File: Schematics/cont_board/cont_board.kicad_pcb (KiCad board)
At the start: 2 copper layers, 238 x 67 mm, 45 parts, among them IC1 LM2931AZ-5.0_TO92, J1 Conn_01x04, J2 Conn_01x04, J3 Conn_01x04, J4 Conn_01x04, Q1 BD438, Q2 BD438, Q3 BD438, SW1 SW_SPDT, U1 LM317_TO-220, U2 MCP23017_SP, U3 ULN2803A, U4 MCP23017_SP, U5 ULN2803A

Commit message: Lamp Board Schematic started
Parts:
- moved H6 22.0 mm to (174.5, 83.5)
- moved H4 20.0 mm to (118.5, 103.5)
- moved U4 9.52 mm to (186.1, 66.0)
- moved JP4 5.85 mm to (188.0, 108.6)
- moved JP5 5.85 mm to (188.0, 111.8)
- moved JP6 5.85 mm to (188.0, 114.9)
- moved U5 4.44 mm to (200.7, 92.7)
- moved U3 4.44 mm to (200.7, 66.0)
- moved C6 0.63 mm to (124.5, 92.1)
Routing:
- net +5V: track 312.4 -> 333.8 mm, vias 3 -> 2
- net SCL: track 181.5 -> 194.8 mm, vias 3 -> 4
- net SDA: track 181.8 -> 194.4 mm, vias 1 -> 2
- net GND: track 26.5 -> 14.7 mm
- net LC6: track 58.6 -> 51.0 mm, vias 1 -> 0
- net LC9: track 41.1 -> 34.3 mm
- net CAM2_POS: track 94.7 -> 99.9 mm
- net LC2: track 14.1 -> 9.09 mm
- net LC3: track 14.1 -> 9.09 mm
- net LC1: track 14.1 -> 9.09 mm
- net LR1: track 22.6 -> 18.0 mm
- net /lamp_drive/c7: track 64.4 -> 60.0 mm
- net /lamp_drive/c5: track 64.8 -> 60.4 mm
- net /lamp_drive/r1: track 28.7 -> 24.3 mm
- net /lamp_drive/c6: track 64.4 -> 60.0 mm
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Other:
- board text added: "04/12/2023 - last rev. 07/12/2023"
- board text added: "CUED | LZB - Enigma Control Board v1.2"
- board text removed: "04/12/2023 - last rev. 06/12/2023"
- board text removed: "CUED | LZB - Enigma Control Board v1.1"

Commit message: Lamp Board Work and drl2dxf
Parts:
- moved H4 5.00 mm to (118.5, 108.5)
- moved H6 2.00 mm to (174.5, 85.5)
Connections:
- net Net-(IC1-VI) renamed /smth
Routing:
- net CAM2_POS: track 99.9 -> 94.2 mm
- net TEST_SW: track 136.4 -> 133.1 mm
- net +12V: track 47.4 -> 46.8 mm
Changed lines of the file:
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@@
   (net 105 "unconnected-(A1-PadVIN)")
   (net 106 "/lamp_drive/hp_r2")
-  (net 107 "Net-(IC1-VI)")
+  (net 107 "/smth")
   (net 108 "/s_a2")
   (net 109 "/s_a1")
@@
   )
   (footprint "MountingHole:MountingHole_3.2mm_M3_Pad_Via" (layer "F.Cu")
-    (at 118.5 103.5)
+    (at 118.5 108.5)
     (descr "Mounting Hole 3.2mm, M3")
     (tags "mounting hole 3.2mm m3")
@@
       (net 8 "+12V") (pintype "passive"))
     (pad "2" thru_hole oval (at 10.16 0 90) (size 1.6 1.6) (drill 0.8) (layers "*.Cu" "*.Mask")
-      (net 107 "Net-(IC1-VI)") (pintype "passive"))
+      (net 107 "/smth") (pintype "passive"))
     (model "${KICAD6_3DMODEL_DIR}/Resistor_THT.3dshapes/R_Axial_DIN0207_L6.3mm_D2.5mm_P10.16mm_Horizontal.wrl"
       (offset (xyz 0 0 0))
@@
       (stroke (width 0.1) (type solid)) (layer "F.Fab"))
     (pad "1" thru_hole circle (at 0 0 90) (size 1.6 1.6) (drill 0.8) (layers "*.Cu" "*.Mask")
-      (net 107 "Net-(IC1-VI)") (pintype "passive"))
+      (net 107 "/smth") (pintype "passive"))
     (pad "2" thru_hole circle (at 5 0 90) (size 1.6 1.6) (drill 0.8) (layers "*.Cu" "*.Mask")
       (net 1 "GND") (pintype "passive"))
@@
   )
   (footprint "MountingHole:MountingHole_3.2mm_M3_Pad_Via" (layer "F.Cu")
-    (at 174.5 83.5)
+    (at 174.5 85.5)
     (descr "Mounting Hole 3.2mm, M3")
     (tags "mounting hole 3.2mm m3")
@@
       (net 1 "GND") (pinfunction "GND") (pintype "power_in"))
     (pad "3" thru_hole oval (at 2.54 0 270) (size 1.05 1.5) (drill 0.75) (layers "*.Cu" "*.Mask")
-      (net 107 "Net-(IC1-VI)") (pinfunction "VI") (pintype "power_in"))
+      (net 107 "/smth") (pinfunction "VI") (pintype "power_in"))
     (model "${KICAD6_3DMODEL_DIR}/Package_TO_SOT_THT.3dshapes/TO-92_Inline.wrl"
       (offset (xyz 0 0 0))
@@
   (via (at 182.88 91.44) (size 1.2) (drill 0.6) (layers "F.Cu" "B.Cu") (free) (net 1))
   (via (at 231.14 80.09) (size 1.2) (drill 0.6) (layers "F.Cu" "B.Cu") (free) (net 1))
+  (segment (start 125.73 101.6) (end 125.73 102.87) (width 0.5) (layer "F.Cu") (net 2))
+  (segment (start 130.81 107.95) (end 132.08 107.95) (width 0.5) (layer "F.Cu") (net 2))
   (segment (start 132.08 107.95) (end 135.89 104.14) (width 0.5) (layer "F.Cu") (net 2))
-  (segment (start 125.73 107.315) (end 126.365 107.95) (width 0.5) (layer "F.Cu") (net 2))
-  (segment (start 126.365 107.95) (end 132.08 107.95) (width 0.5) (layer "F.Cu") (net 2))
   (segment (start 135.89 104.14) (end 135.89 92.075) (width 0.5) (layer "F.Cu") (net 2))
-  (segment (start 125.73 100.33) (end 125.73 107.315) (width 0.5) (layer "F.Cu") (net 2))
+  (segment (start 125.73 102.87) (end 130.81 107.95) (width 0.5) (layer "F.Cu") (net 2))
   (via (at 135.89 92.075) (size 0.8) (drill 0.4) (layers "F.Cu" "B.Cu") (net 2))
-  (via (at 125.73 100.33) (size 0.8) (drill 0.4) (layers "F.Cu" "B.Cu") (net 2))
-  (segment (start 86.36 106.68) (end 77.47 115.57) (width 0.5) (layer "B.Cu") (net 2))
-  (segment (start 91.44 104.14) (end 88.9 106.68) (width 0.5) (layer "B.Cu") (net 2))
+  (via (at 125.73 101.6) (size 0.8) (drill 0.4) (layers "F.Cu" "B.Cu") (net 2))
+  (segment (start 125.095 101.6) (end 118.11 94.615) (width 0.5) (layer "B.Cu") (net 2))
   (segment (start 138.43 89.535) (end 143.51 89.535) (width 0.5) (layer "B.Cu") (net 2))
-  (segment (start 50.8 115.57) (end 53.34 113.03) (width 0.5) (layer "B.Cu") (net 2))
   (segment (start 118.11 94.615) (end 97.79 94.615) (width 0.5) (layer "B.Cu") (net 2))
+  (segment (start 50.8 115.57) (end 53.34 113.03) (width 0.5) (layer "B.Cu") (net 2))
+  (segment (start 125.73 101.6) (end 125.095 101.6) (width 0.5) (layer "B.Cu") (net 2))
   (segment (start 77.47 115.57) (end 50.8 115.57) (width 0.5) (layer "B.Cu") (net 2))
   (segment (start 50.8 115.57) (end 47.27 119.1) (width 0.5) (layer "B.Cu") (net 2))
-  (segment (start 123.825 100.33) (end 118.11 94.615) (width 0.5) (layer "B.Cu") (net 2))
-  (segment (start 47.27 119.1) (end 47.27 119.38) (width 0.5) (layer "B.Cu") (net 2))
   (segment (start 97.79 94.615) (end 91.44 100.965) (width 0.5) (layer "B.Cu") (net 2))
+  (segment (start 47.27 119.1) (end 47.27 119.38) (width 0.5) (layer "B.Cu") (net 2))
   (segment (start 91.44 100.965) (end 91.44 104.14) (width 0.5) (layer "B.Cu") (net 2))
-  (segment (start 135.89 92.075) (end 138.43 89.535) (width 0.5) (layer "B.Cu") (net 2))
+  (segment (start 86.36 106.68) (end 77.47 115.57) (width 0.5) (layer "B.Cu") (net 2))
   (segment (start 88.9 106.68) (end 86.36 106.68) (width 0.5) (layer "B.Cu") (net 2))
-  (segment (start 125.73 100.33) (end 123.825 100.33) (width 0.5) (layer "B.Cu") (net 2))
+  (segment (start 91.44 104.14) (end 88.9 106.68) (width 0.5) (layer "B.Cu") (net 2))
+  (segment (start 135.89 92.075) (end 138.43 89.535) (width 0.5) (layer "B.Cu") (net 2))
   (segment (start 134.62 90.805) (end 135.89 89.535) (width 0.5) (layer "F.Cu") (net 3))
   (segment (start 131.38 105.98) (end 132.145 105.98) (width 0.5) (layer "F.Cu") (net 3))
@@
   (via (at 132.08 104.14) (size 0.8) (drill 0.4) (layers "F.Cu" "B.Cu") (net 4))
   (via (at 133.35 87.63) (size 0.8) (drill 0.4) (layers "F.Cu" "B.Cu") (net 4))
-  (segment (start 109.22 97.155) (end 112.395 100.33) (width 0.5) (layer "B.Cu") (net 4))
-  (segment (start 115.57 107.95) (end 128.27 107.95) (width 0.5) (layer "B.Cu") (net 4))
-  (segment (start 128.27 107.95) (end 132.08 104.14) (width 0.5) (layer "B.Cu") (net 4))
   (segment (start 95.885 103.505) (end 102.235 97.155) (width 0.5) (layer "B.Cu") (net 4))
+  (segment (start 102.235 97.155) (end 116.84 97.155) (width 0.5) (layer "B.Cu") (net 4))
   (segment (start 137.795 80.01) (end 142.24 84.455) (width 0.5) (layer "B.Cu") (net 4))
   (segment (start 133.35 81.915) (end 135.255 80.01) (width 0.5) (layer "B.Cu") (net 4))
-  (segment (start 112.395 100.33) (end 112.395 104.775) (width 0.5) (layer "B.Cu") (net 4))
   (segment (start 93.345 119.38) (end 95.885 116.84) (width 0.5) (layer "B.Cu") (net 4))
-  (segment (start 102.235 97.155) (end 109.22 97.155) (width 0.5) (layer "B.Cu") (net 4))
+  (segment (start 116.84 97.155) (end 123.825 104.14) (width 0.5) (layer "B.Cu") (net 4))
   (segment (start 142.24 84.455) (end 143.51 84.455) (width 0.5) (layer "B.Cu") (net 4))
   (segment (start 135.255 80.01) (end 137.795 80.01) (width 0.5) (layer "B.Cu") (net 4))
-  (segment (start 112.395 104.775) (end 115.57 107.95) (width 0.5) (layer "B.Cu") (net 4))
   (segment (start 95.885 116.84) (end 95.885 103.505) (width 0.5) (layer "B.Cu") (net 4))
   (segment (start 133.35 87.63) (end 133.35 81.915) (width 0.5) (layer "B.Cu") (net 4))
+  (segment (start 123.825 104.14) (end 132.08 104.14) (width 0.5) (layer "B.Cu") (net 4))
   (segment (start 152.4 75.565) (end 152.4 94.615) (width 0.5) (layer "F.Cu") (net 5))
   (segment (start 184.15 95.25) (end 185.42 96.52) (width 0.5) (layer "F.Cu") (net 5))
@@
   (segment (start 136.525 104.14) (end 132.08 99.695) (width 1) (layer "B.Cu") (net 7))
   (segment (start 132.08 92.075) (end 128.27 92.075) (width 1) (layer "B.Cu") (net 7))
+  (segment (start 108.585 109.22) (end 91.215 109.22) (width 1.2) (layer "F.Cu") (net 8))
   (segment (start 87.63 102.170113) (end 83.755113 102.170113) (width 1.2) (layer "F.Cu") (net 8))
   (segment (start 83.755113 102.170113) (end 79.375 97.79) (width 1.2) (layer "F.Cu") (net 8))
-  (segment (start 116.84 115.57) (end 116.84 114.505) (width 1.2) (layer "F.Cu") (net 8))
-  (segment (start 91.215 109.22) (end 111.555 109.22) (width 1.2) (layer "F.Cu") (net 8))
-  (segment (start 116.84 114.505) (end 111.555 109.22) (width 1.2) (layer "F.Cu") (net 8))
+  (segment (start 114.935 115.57) (end 108.585 109.22) (width 1.2) (layer "F.Cu") (net 8))
   (segment (start 87.63 105.635) (end 91.215 109.22) (width 1.2) (layer "F.Cu") (net 8))
   (segment (start 87.63 102.235) (end 87.63 105.635) (width 1.2) (layer "F.Cu") (net 8))
+  (segment (start 116.84 115.57) (end 114.935 115.57) (width 1.2) (layer "F.Cu") (net 8))
   (segment (start 69.215 115.57) (end 69.215 109.22) (width 1.2) (layer "F.Cu") (net 9))
   (segment (start 73.025 119.38) (end 69.215 115.57) (width 1.2) (layer "F.Cu") (net 9))

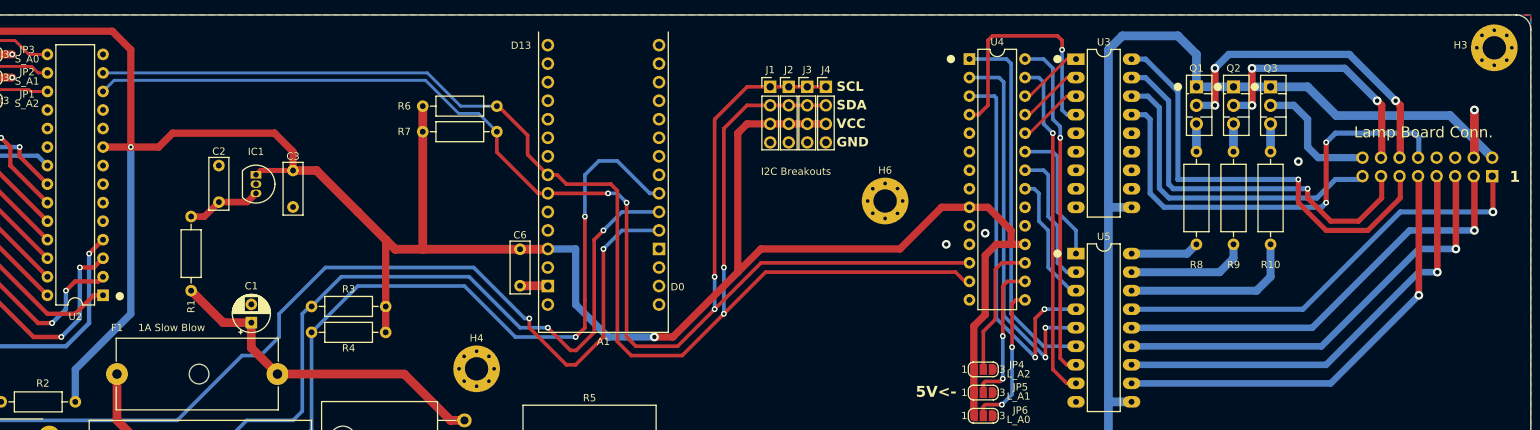
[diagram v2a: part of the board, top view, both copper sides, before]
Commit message: Fixed error - mcp rst tied to gnd
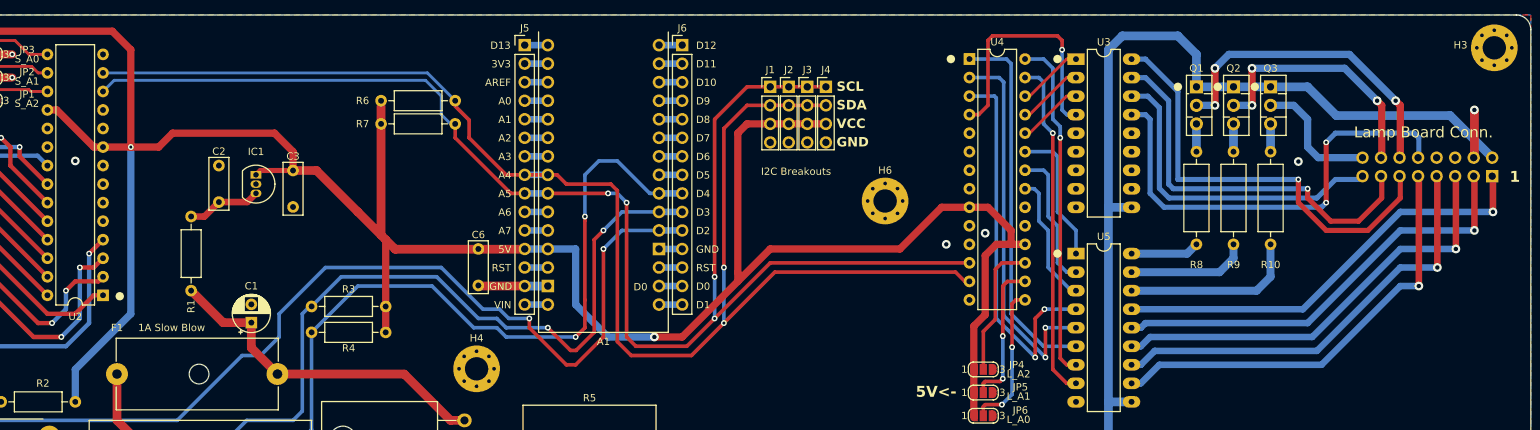
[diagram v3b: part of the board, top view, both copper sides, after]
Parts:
- added J5: Conn_01x15, Connector_PinHeader_2.54mm:PinHeader_1x15_P2.54mm_Vertical, F.Cu at (125.1, 64.1)
- added J6: Conn_01x15, Connector_PinHeader_2.54mm:PinHeader_1x15_P2.54mm_Vertical, F.Cu at (146.7, 64.1)
- R5: value 3R0 -> 2R7
- moved R7 5.81 mm to (105.4, 74.9)
- moved R6 5.76 mm to (105.4, 71.8)
- moved C6 5.72 mm to (118.7, 92.1)
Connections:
- A1 pad 3V3: unconnected-(A1-3.3V-Pad3V3) -> 3V3
- A1 pad A0: unconnected-(A1-PadA0) -> A0
- A1 pad A1: unconnected-(A1-PadA1) -> A1
- A1 pad A2: unconnected-(A1-PadA2) -> A2
- A1 pad A3: unconnected-(A1-PadA3) -> A3
- A1 pad A6: unconnected-(A1-PadA6) -> A6
- A1 pad A7: unconnected-(A1-PadA7) -> A7
- A1 pad AREF: unconnected-(A1-PadAREF) -> AREF
- A1 pad D0: unconnected-(A1-D0/RX-PadD0) -> D0
- A1 pad D1: unconnected-(A1-D1/TX-PadD1) -> D1
- A1 pad D10: unconnected-(A1-PadD10) -> D10
- A1 pad D11: unconnected-(A1-D11_MOSI-PadD11) -> D11
- A1 pad D12: unconnected-(A1-D12_MISO-PadD12) -> D12
- A1 pad D13: unconnected-(A1-D13_SCK-PadD13) -> D13
- A1 pad D5: unconnected-(A1-PadD5) -> D5
- A1 pad D6: unconnected-(A1-PadD6) -> D6
- A1 pad D7: unconnected-(A1-PadD7) -> D7
- A1 pad D8: unconnected-(A1-PadD8) -> D8
- A1 pad D9: unconnected-(A1-PadD9) -> D9
- A1 pad RST1: unconnected-(A1-RESET-PadRST1) -> RST1
- A1 pad RST2: unconnected-(A1-RESET-PadRST2) -> RST2
- A1 pad VIN: unconnected-(A1-PadVIN) -> VIN
- U2 pad 18: GND -> +5V
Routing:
- net +5V: track 333.8 -> 342.9 mm
- net GND: track 14.7 -> 23.6 mm, vias 6 -> 7
- net SDA: track 194.4 -> 198.4 mm
- net VIN: track 0.00 -> 3.18 mm
- net TEST_SW: track 133.1 -> 136.3 mm
- net RST2: track 0.00 -> 3.18 mm
- net RST1: track 0.00 -> 3.18 mm
- net D9: track 0.00 -> 3.18 mm
- net D8: track 0.00 -> 3.18 mm
- net D7: track 0.00 -> 3.18 mm
- net D6: track 0.00 -> 3.18 mm
- net D5: track 0.00 -> 3.18 mm
- net D13: track 0.00 -> 3.18 mm
- net D12: track 0.00 -> 3.18 mm
- net D11: track 0.00 -> 3.18 mm
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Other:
- board text added: "3V3"
- board text added: "5V"
- board text added: "A0"
- board text added: "A1"
- board text added: "A2"
- board text added: "A3"
- board text added: "A4"
- board text added: "A5"
- board text added: "A6"
- board text added: "A7"
- board text added: "AREF"
- board text added: "D0"
- board text added: "D1"
- board text added: "D10"
- board text added: "D11"
- board text added: "D12"
- board text added: "D2"
- board text added: "D3"
- board text added: "D4"
- board text added: "D5"
- board text added: "D6"
- board text added: "D7"
- board text added: "D8"
- board text added: "D9"
- board text added: "RST"
- board text added: "VIN"

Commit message: Final Commit
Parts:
- added C10: 100n, Capacitor_SMD:C_0603_1608Metric, F.Cu at (176.1, 109.4)
- added C4: 10u, Capacitor_SMD:C_0603_1608Metric, F.Cu at (167.5, 109.5)
- added C5: 100n, Capacitor_SMD:C_0603_1608Metric, F.Cu at (166.0, 109.5)
- added C7: 10u, Capacitor_SMD:C_0603_1608Metric, F.Cu at (157.1, 109.5)
- added C8: 100n, Capacitor_SMD:C_0603_1608Metric, F.Cu at (155.4, 109.5)
- added C9: 10u, Capacitor_SMD:C_0603_1608Metric, F.Cu at (177.7, 109.4)
- added J10: Conn_01x03, Connector_PinHeader_2.54mm:PinHeader_1x03_P2.54mm_Vertical, F.Cu at (166.6, 102.1)
- added J11: Conn_01x03, Connector_PinHeader_2.54mm:PinHeader_1x03_P2.54mm_Vertical, F.Cu at (176.8, 102.1)
- added J12: Conn_01x03, user_global_footprints:TerminalBlock_bornier-3_P5.08mm_slim, F.Cu at (188.6, 119.4)
- added J13: Conn_02x03_Counter_Clockwise, user_global_footprints:PinHeader_2x03_P2.54mm_Horizontal_Short_Pins, B.Cu at (132.1, 114.8)
- added J7: Conn_01x03, Connector_PinHeader_2.54mm:PinHeader_1x03_P2.54mm_Vertical, F.Cu at (156.3, 102.1)
- added J8: Conn_01x03, user_global_footprints:TerminalBlock_bornier-3_P5.08mm_slim, F.Cu at (158.1, 119.4)
- added J9: Conn_01x03, user_global_footprints:TerminalBlock_bornier-3_P5.08mm_slim, F.Cu at (173.4, 119.4)
- added U6: ATtiny202-SS, Package_SO:SOIC-8_3.9x4.9mm_P1.27mm, F.Cu at (171.1, 107.8)
- added U7: ATtiny202-SS, Package_SO:SOIC-8_3.9x4.9mm_P1.27mm, F.Cu at (160.8, 107.8)
- added U8: ATtiny202-SS, Package_SO:SOIC-8_3.9x4.9mm_P1.27mm, F.Cu at (181.2, 107.7)
- H1, H2, H3, H4, H5, H6: footprint MountingHole:MountingHole_3.2mm_M3_Pad_Via -> user_global_footprints:MountingHole_4mm_Pad_Via
- J4: value Conn_01x04 -> PBOARD_CONN; footprint user_global_footprints:PinHeader_1x04_P2.54mm_Vertical_SLIM -> Connector_PinHeader_2.54mm:PinHeader_1x04_P2.54mm_Horizontal
- moved J4 78.1 mm to (88.3, 70.4), turned to 90 degrees
- moved R4 23.6 mm to (119.4, 100.8), turned to 90 degrees
- moved R3 20.2 mm to (116.1, 100.8), turned to 90 degrees
- moved R6 15.3 mm to (113.8, 84.6)
- moved R7 10.7 mm to (113.8, 81.5)
- moved C6 7.49 mm to (126.2, 92.2)
- moved A1 4.83 mm to (140.7, 60.5)
- moved J5 4.83 mm to (129.9, 64.3)
- moved J6 4.83 mm to (151.5, 64.3)
- moved Q1 1.43 mm to (217.8, 68.6)
- moved R8 1.43 mm to (217.8, 90.2)
- moved JP5 1.43 mm to (188.6, 110.5)
- moved JP6 1.43 mm to (188.6, 113.7)
- moved Q2 1.43 mm to (222.9, 68.6)
- moved Q3 1.43 mm to (228.0, 68.6)
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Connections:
- A1 pad VIN: VIN -> unconnected-(A1-PadVIN)
- J5 pad 15: VIN -> unconnected-(J5-Pin_15-Pad15)
- R6 pad 2: SDA -> SCL
- R7 pad 2: SCL -> SDA
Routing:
- net +5V: track 342.9 -> 426.3 mm, vias 2 -> 6
- net D13: track 3.18 -> 64.5 mm, vias 0 -> 2
- net D12: track 3.18 -> 60.4 mm, vias 0 -> 2
- net D11: track 3.18 -> 56.3 mm, vias 0 -> 2
- net SDA: track 198.4 -> 230.3 mm, vias 2 -> 5
- net RST2: track 3.18 -> 24.8 mm, vias 0 -> 1
- net SCL: track 197.0 -> 218.4 mm
- net /RotorEncoder2/r_encb: track 0.00 -> 18.3 mm
- net /RotorEncoder2/r_enca: track 0.00 -> 14.5 mm
- net GND: track 23.6 -> 37.7 mm, vias 7 -> 29
- net /RotorEncoder/r_encb: track 0.00 -> 10.8 mm
- net /RotorEncoder/r_enca: track 0.00 -> 10.4 mm
- net /RotorEncoder1/r_enca: track 0.00 -> 9.99 mm
- net /RotorEncoder1/r_encb: track 0.00 -> 9.88 mm
- net +12VA: track 214.6 -> 224.0 mm
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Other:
- board text added: "+a-"
- board text added: "04/12/2023 - last rev. 30/03/2024"
- board text added: "B1"
- board text added: "B2"
- board text added: "B3"
- board text added: "CUED | LZB - Enigma Control Board v2.0"
- board text added: "Com"
- board text added: "F1"
- board text added: "LAMP BOARD"
- board text added: "ROTORS"
- board text added: "SWITCH BOARD"
- board text added: "TOWARDS ROTORS"
- board text removed: "04/12/2023 - last rev. 07/12/2023"
- board text removed: "3V3"
- board text removed: "5V"
- board text removed: "5V<-"
- board text removed: "A0"
- board text removed: "A4"
- board text removed: "A5"
- board text removed: "A6"
- board text removed: "A7"
- board text removed: "AREF"
- board text removed: "CUED | LZB - Enigma Control Board v1.2"
- board text removed: "D0"
- board text removed: "D1"
- board text removed: "D10"
- board text removed: "D11"
- board text removed: "D12"
- board text removed: "D2"
- board text removed: "D3"
- board text removed: "D4"
- board text removed: "D5"
- board text removed: "D6"
- board text removed: "D7"
- board text removed: "D8"
- board text removed: "D9"
- board text removed: "Lamp Board Conn."
- board text removed: "RST"
- board text removed: "Switch Board Conn."
- board text removed: "VIN"
